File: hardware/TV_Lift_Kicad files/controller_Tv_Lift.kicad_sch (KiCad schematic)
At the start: 97 parts, among them J1 socket LAN8720a, J10 CONN_IR_OUT, J11 DRY CONTACT UP DOWN, J12 DRY CONTACT, J2 POWER 24V, J3 CAN_bus, J4 ENCODER, J5 ENCODER_POWER, J6 CONN_RS232, J7 M1 LIMIT UP DOWN, J8 Signal PWR, J9 MOTOR_OUT, Q1 2N3904, SW1 UP, SW2 DOWN, SW3 STOP, SW4 Reset, U1 MAX3232, U10 VNH5019A-E, U2 TSOP32S40F, U3 SN65HVD230, U4 ESP32-WROOM-32, U5 LM2596S-5, U6 AMS1117-3.3, U7 PC817, U8 PC817, U9 NCS1S1205SC

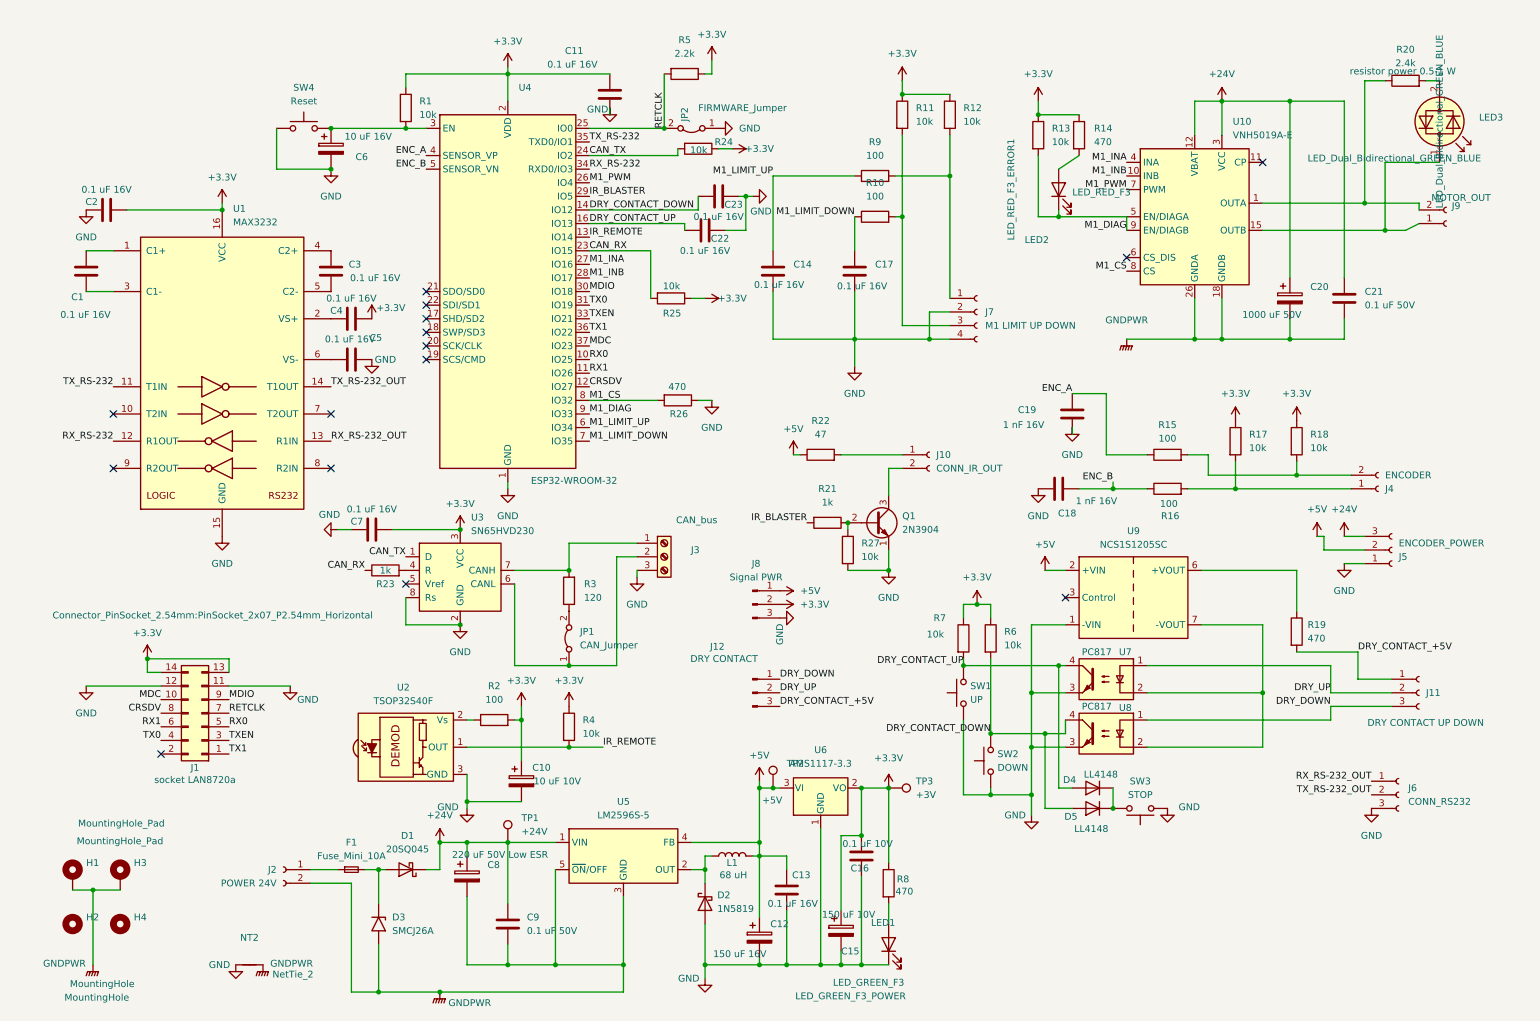
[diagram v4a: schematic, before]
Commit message: fix bom list of connectors
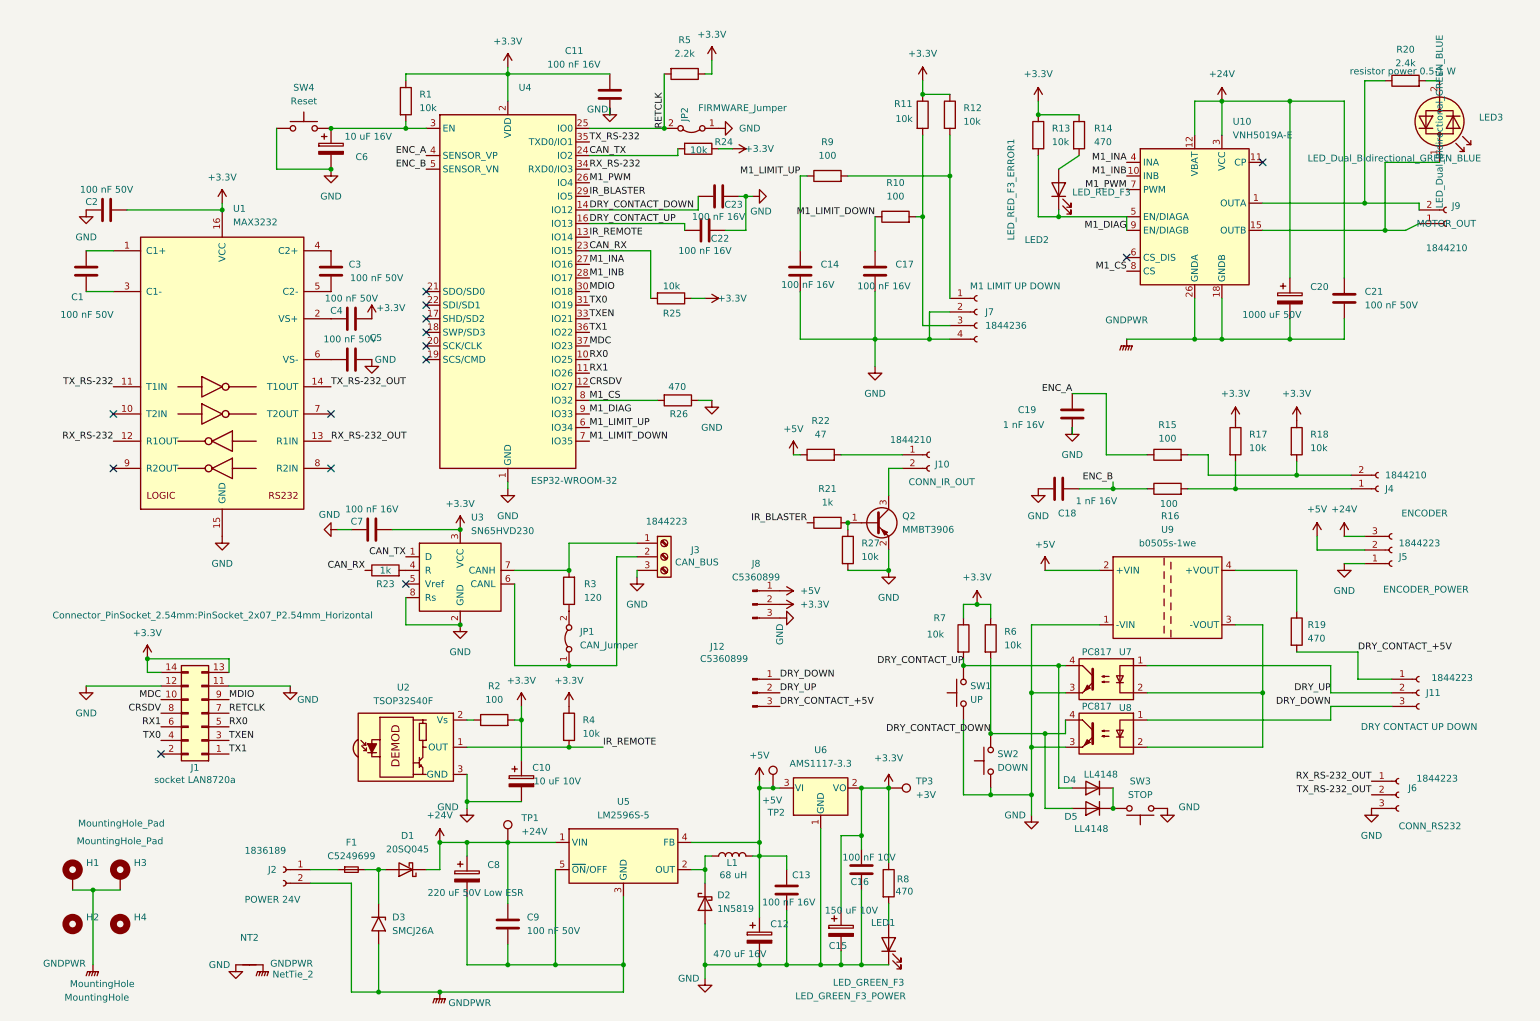
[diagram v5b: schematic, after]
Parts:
- removed Q1: 2N3904, Package_TO_SOT_THT:TO-92_Inline, symbol Transistor_BJT:2N3904
- added Q2: MMBT3906, Package_TO_SOT_SMD:SOT-23, symbol Transistor_BJT:MMBT3906
- C1, C2, C3, C4, C5: value 0.1 uF 16V -> 100 nF 50V
- C11, C13, C14, C17, C22, C23, C7: value 0.1 uF 16V -> 100 nF 16V
- C12: value 150 uF 16V -> 470 uF 16V
- C16: value 0.1 uF 10V -> 100 nF 10V
- C21, C9: value 0.1 uF 50V -> 100 nF 50V
- C6: footprint Capacitor_THT:CP_Radial_D5.0mm_P2.00mm -> Capacitor_SMD:C_0805_2012Metric
- F1: value Fuse_Mini_10A -> C5249699
- J10: value CONN_IR_OUT -> 1844210
- J11: value DRY CONTACT UP DOWN -> 1844223
- J12: value DRY CONTACT -> C5360899
- J2: value POWER 24V -> 1836189
- J3: value CAN_bus -> 1844223
- J4: value ENCODER -> 1844210
- J5: value ENCODER_POWER -> 1844223
- J6: value CONN_RS232 -> 1844223
- J7: value M1 LIMIT UP DOWN -> 1844236
- J8: value Signal PWR -> C5360899
- J9: value MOTOR_OUT -> 1844210
- U9: value NCS1S1205SC -> b0505s-1we; footprint Converter_DCDC:Converter_DCDC_Murata_NCS1SxxxxSC_THT -> Converter_DCDC:Converter_DCDC_RECOM_R-78S-0.1_THT; symbol Converter_DCDC:NCS1S1205SC -> Regulator_Switching:CRE1S0505SC
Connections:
- net GND: now also Q2.2 (E)
- net at R21.1, R27.1: now also Q2.1 (B)
- net at J10.2 (Pin_2): now also Q2.3 (C)
- net at U7.2, U8.2: now also U9.3 (-VOUT); no longer U9.7 (-VOUT)
- net at R19.1: now also U9.4 (+VOUT); no longer U9.6 (+VOUT)
- no-connect marks 15 -> 14
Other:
- moved on the sheet: C14, C16, C17, R1, R10, R11, R9

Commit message: done boardConfig.h
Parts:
- C14, C17: value 100 nF 16V -> 100 nF 50V
- C18, C19: value 1 nF 16V -> 1 nF 50V
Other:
- moved on the sheet: C14, R9
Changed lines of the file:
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@@
 	)
 	(junction
+		(at 182.88 40.64)
+		(diameter 0)
+		(color 0 0 0 0)
+	)
+	(junction
 		(at 91.44 106.68)
 		(diameter 0)
@@
 	)
 	(junction
-		(at 182.88 40.64)
-		(diameter 0)
-		(color 0 0 0 0)
-	)
-	(junction
 		(at 179.07 71.12)
 		(diameter 0)
@@
 	(wire
 		(pts
-			(xy 154.94 71.12) (xy 168.91 71.12)
+			(xy 158.75 71.12) (xy 168.91 71.12)
 		)
 		(stroke
@@
 	(wire
 		(pts
-			(xy 163.83 40.64) (xy 182.88 40.64)
+			(xy 167.64 40.64) (xy 182.88 40.64)
 		)
 		(stroke
@@
 	(wire
 		(pts
-			(xy 154.94 62.23) (xy 154.94 71.12)
+			(xy 158.75 62.23) (xy 158.75 71.12)
 		)
 		(stroke
@@
 	(wire
 		(pts
-			(xy 154.94 40.64) (xy 156.21 40.64)
+			(xy 158.75 40.64) (xy 160.02 40.64)
 		)
 		(stroke
@@
 	(wire
 		(pts
-			(xy 154.94 40.64) (xy 154.94 54.61)
+			(xy 158.75 40.64) (xy 158.75 54.61)
 		)
 		(stroke
@@
 	)
 	(label "M1_LIMIT_UP"
-		(at 154.94 40.64 180)
+		(at 158.75 40.64 180)
 		(effects
 			(font
@@
 			)
 		)
-		(property "Value" "1 nF 16V"
+		(property "Value" "1 nF 50V"
 			(at 214.122 101.346 90)
 			(show_name no)
@@
 		)
 		(property "Description" "ENCODER"
-			(at 271.526 103.632 0)
+			(at 265.938 92.202 0)
 			(show_name no)
 			(do_not_autoplace no)
@@
 			)
 		)
-		(property "Value" "1 nF 16V"
+		(property "Value" "1 nF 50V"
 			(at 192.786 87.122 0)
 			(show_name no)
@@
 	(symbol
 		(lib_id "Device:R")
-		(at 160.02 40.64 90)
+		(at 163.83 40.64 90)
 		(unit 1)
 		(body_style 1)
@@
 		(fields_autoplaced yes)
 		(property "Reference" "R9"
-			(at 160.02 34.29 90)
+			(at 163.83 34.29 90)
 			(show_name no)
 			(do_not_autoplace no)
@@
 		)
 		(property "Value" "100"
-			(at 160.02 36.83 90)
+			(at 163.83 36.83 90)
 			(show_name no)
 			(do_not_autoplace no)
@@
 		)
 		(property "Footprint" "Resistor_SMD:R_0805_2012Metric"
-			(at 160.02 42.418 90)
+			(at 163.83 42.418 90)
 			(hide yes)
 			(show_name no)
@@
 		)
 		(property "Datasheet" ""
-			(at 160.02 40.64 0)
+			(at 163.83 40.64 0)
 			(hide yes)
 			(show_name no)
@@
 		)
 		(property "Description" ""
-			(at 160.02 40.64 0)
+			(at 163.83 40.64 0)
 			(show_name no)
 			(do_not_autoplace no)
@@
 	(symbol
 		(lib_id "Device:C")
-		(at 154.94 58.42 0)
+		(at 158.75 58.42 0)
 		(unit 1)
 		(body_style 1)
@@
 		(dnp no)
 		(property "Reference" "C14"
-			(at 158.75 57.1499 0)
+			(at 166.37 57.1499 0)
 			(show_name no)
 			(do_not_autoplace no)
@@
 			)
 		)
-		(property "Value" "100 nF 16V"
-			(at 151.384 60.96 0)
+		(property "Value" "100 nF 50V"
+			(at 155.194 60.96 0)
 			(show_name no)
 			(do_not_autoplace no)
@@
 		)
 		(property "Footprint" "Capacitor_SMD:C_0805_2012Metric"
-			(at 155.9052 62.23 0)
+			(at 159.7152 62.23 0)
 			(hide yes)
 			(show_name no)
@@
 		)
 		(property "Datasheet" ""
-			(at 154.94 58.42 0)
+			(at 158.75 58.42 0)
 			(hide yes)
 			(show_name no)
@@
 		)
 		(property "Description" ""
-			(at 154.94 58.42 0)
+			(at 158.75 58.42 0)
 			(show_name no)
 			(do_not_autoplace no)
@@
 			)
 		)
-		(property "Value" "100 nF 16V"
+		(property "Value" "100 nF 50V"
 			(at 165.608 61.214 0)
 			(show_name no)

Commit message: fix input manager: correct limit switch logic and remove unnecessary comments
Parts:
- added TP4: Signal GND, TestPoint:TestPoint_Pad_D2.0mm, symbol Connector:TestPoint
- added TP5: GNDPWR, TestPoint:TestPoint_Pad_D2.0mm, symbol Connector:TestPoint
- SW1: value UP -> TS-1187A-BAB; footprint Button_Switch_THT:SW_PUSH_6mm -> Button_Switch_SMD:SW_Push_1P1T_XKB_TS-1187A
- SW2: value DOWN -> TS-1187A-BAB; footprint Button_Switch_THT:SW_PUSH_6mm -> Button_Switch_SMD:SW_Push_1P1T_XKB_TS-1187A
- SW3: value STOP -> TS-1187A-BAB; footprint Button_Switch_THT:SW_PUSH_6mm -> Button_Switch_SMD:SW_Push_1P1T_XKB_TS-1187A
- SW4: value Reset -> TS-1187A-BAB; footprint Button_Switch_THT:SW_PUSH_6mm -> Button_Switch_SMD:SW_Push_1P1T_XKB_TS-1187A
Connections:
- net GND: now also TP4.1
- net GNDPWR: now also TP5.1
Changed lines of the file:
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@@
 	)
 	(junction
-		(at 100.33 21.59)
+		(at 100.33 20.32)
 		(diameter 0)
 		(color 0 0 0 0)
@@
 	)
 	(junction
+		(at 156.21 187.96)
+		(diameter 0)
+		(color 0 0 0 0)
+	)
+	(junction
 		(at 228.6 71.12)
 		(diameter 0)
@@
 	)
 	(junction
+		(at 81.28 193.04)
+		(diameter 0)
+		(color 0 0 0 0)
+	)
+	(junction
 		(at 200.66 144.78)
 		(diameter 0)
@@
 	(wire
 		(pts
-			(xy 100.33 20.32) (xy 100.33 21.59)
-		)
-		(stroke
-			(width 0)
-			(type default)
-		)
-	)
-	(wire
-		(pts
 			(xy 144.78 50.8) (xy 140.97 50.8)
 		)
@@
 	(wire
 		(pts
-			(xy 137.16 187.96) (xy 158.75 187.96)
+			(xy 137.16 187.96) (xy 156.21 187.96)
 		)
 		(stroke
@@
 	(wire
 		(pts
-			(xy 81.28 22.86) (xy 81.28 21.59)
+			(xy 81.28 22.86) (xy 81.28 20.32)
 		)
 		(stroke
@@
 	(wire
 		(pts
-			(xy 119.38 21.59) (xy 100.33 21.59)
+			(xy 119.38 20.32) (xy 100.33 20.32)
 		)
 		(stroke
@@
 	(wire
 		(pts
-			(xy 81.28 21.59) (xy 100.33 21.59)
+			(xy 81.28 20.32) (xy 100.33 20.32)
 		)
 		(stroke
@@
 	(wire
 		(pts
+			(xy 81.28 193.04) (xy 87.63 193.04)
+		)
+		(stroke
+			(width 0)
+			(type default)
+		)
+	)
+	(wire
+		(pts
+			(xy 119.38 20.32) (xy 119.38 21.59)
+		)
+		(stroke
+			(width 0)
+			(type default)
+		)
+	)
+	(wire
+		(pts
 			(xy 71.12 193.04) (xy 76.2 193.04)
 		)
@@
 	(wire
 		(pts
+			(xy 156.21 187.96) (xy 158.75 187.96)
+		)
+		(stroke
+			(width 0)
+			(type default)
+		)
+	)
+	(wire
+		(pts
 			(xy 101.6 114.3) (xy 111.76 114.3)
 		)
@@
 	(wire
 		(pts
-			(xy 100.33 21.59) (xy 100.33 26.67)
+			(xy 100.33 20.32) (xy 100.33 26.67)
 		)
 		(stroke
@@
 	(wire
 		(pts
-			(xy 76.2 193.04) (xy 87.63 193.04)
+			(xy 76.2 193.04) (xy 81.28 193.04)
 		)
 		(stroke
@@
 		(dnp no)
 		(property "Reference" "C11"
-			(at 110.998 17.272 0)
+			(at 118.618 20.574 0)
 			(show_name no)
 			(do_not_autoplace no)
@@
 		)
 		(property "Value" "100 nF 16V"
-			(at 107.696 19.812 0)
+			(at 115.316 23.114 0)
 			(show_name no)
 			(do_not_autoplace no)
@@
 	)
 	(symbol
+		(lib_id "Connector:TestPoint")
+		(at 81.28 193.04 0)
+		(unit 1)
+		(body_style 1)
+		(exclude_from_sim no)
+		(in_bom yes)
+		(on_board yes)
+		(in_pos_files yes)
+		(dnp no)
+		(property "Reference" "TP5"
+			(at 79.502 195.072 0)
+			(show_name no)
+			(do_not_autoplace no)
+			(effects
+				(font
+					(size 1.27 1.27)
+				)
+				(justify left)
+			)
+		)
+		(property "Value" "GNDPWR"
+			(at 77.978 187.96 0)
+			(show_name no)
+			(do_not_autoplace no)
+			(effects
+				(font
+					(size 1.27 1.27)
+				)
+				(justify left)
+			)
+		)
+		(property "Footprint" "TestPoint:TestPoint_Pad_D2.0mm"
+			(at 86.36 193.04 0)
+			(hide yes)
+			(show_name no)
+			(do_not_autoplace no)
+			(effects
+				(font
+					(size 1.27 1.27)
+				)
+			)
+		)
+		(property "Datasheet" ""
+			(at 86.36 193.04 0)
+			(hide yes)
+			(show_name no)
+			(do_not_autoplace no)
+			(effects
+				(font
+					(size 1.27 1.27)
+				)
+			)
+		)
+		(property "Description" "test point"
+			(at 81.28 193.04 0)
+			(hide yes)
+			(show_name no)
+			(do_not_autoplace no)
+			(effects
+				(font
+					(size 1.27 1.27)
+				)
+			)
+		)
+		(pin "1"
+		)
+		(instances
+			(project "controller_Tv_Lift"
+				(path "/906b0219-e8e2-4a64-a5ea-d0350d472c53"
+					(reference "TP5")
+					(unit 1)
+				)
+			)
+		)
+	)
+	(symbol
 		(lib_id "Switch:SW_Push")
 		(at 62.23 31.75 0)
@@
 			)
 		)
-		(property "Value" "Reset"
+		(property "Value" "TS-1187A-BAB"
 			(at 62.23 26.67 0)
 			(show_name no)
@@
 			)
 		)
-		(property "Footprint" "Button_Switch_THT:SW_PUSH_6mm"
+		(property "Footprint" "Button_Switch_SMD:SW_Push_1P1T_XKB_TS-1187A"
 			(at 62.23 26.67 0)
 			(hide yes)
@@
 			)
 		)
-		(property "Description" "Push button switch, generic, two pins"
+		(property "Description" "RESET"
 			(at 62.23 31.75 0)
 			(hide yes)
@@
 			)
 		)
-		(property "Value" "STOP"
+		(property "Value" "TS-1187A-BAB"
 			(at 218.44 156.21 0)
 			(show_name no)
@@
 			)
 		)
-		(property "Footprint" "Button_Switch_THT:SW_PUSH_6mm"
+		(property "Footprint" "Button_Switch_SMD:SW_Push_1P1T_XKB_TS-1187A"
 			(at 218.44 163.83 0)
 			(hide yes)
@@
 			)
 		)
-		(property "Description" "Push button switch, generic, two pins"
+		(property "Description" "STOP"
 			(at 218.44 158.75 0)
 			(hide yes)
@@
 			)
 		)
-		(property "Value" "UP"
+		(property "Value" "TS-1187A-BAB"
 			(at 186.69 138.4299 90)
 			(show_name no)
@@
 			)
 		)
-		(property "Footprint" "Button_Switch_THT:SW_PUSH_6mm"
+		(property "Footprint" "Button_Switch_SMD:SW_Push_1P1T_XKB_TS-1187A"
 			(at 180.34 137.16 0)
 			(hide yes)
@@
 			)
 		)
-		(property "Description" "Push button switch, generic, two pins"
+		(property "Description" "UP"
 			(at 185.42 137.16 0)
 			(hide yes)
@@
 	)
 	(symbol
+		(lib_id "Connector:TestPoint")
+		(at 156.21 187.96 0)
+		(unit 1)
+		(body_style 1)
+		(exclude_from_sim no)
+		(in_bom yes)
+		(on_board yes)
+		(in_pos_files yes)
+		(dnp no)
+		(property "Reference" "TP4"
+			(at 154.432 189.992 0)
+			(show_name no)
+			(do_not_autoplace no)
+			(effects
+				(font
+					(size 1.27 1.27)
+				)
+				(justify left)
+			)
+		)
+		(property "Value" "Signal GND"
+			(at 149.86 191.516 0)
+			(show_name no)
+			(do_not_autoplace no)
+			(effects
+				(font
+					(size 1.27 1.27)
+				)
+				(justify left)
+			)
+		)
+		(property "Footprint" "TestPoint:TestPoint_Pad_D2.0mm"
+			(at 161.29 187.96 0)
+			(hide yes)
+			(show_name no)
+			(do_not_autoplace no)
+			(effects
+				(font
+					(size 1.27 1.27)
+				)
+			)
+		)
+		(property "Datasheet" ""
+			(at 161.29 187.96 0)
+			(hide yes)
+			(show_name no)
+			(do_not_autoplace no)
+			(effects
+				(font
+					(size 1.27 1.27)
+				)
+			)
+		)
+		(property "Description" "test point"
+			(at 156.21 187.96 0)
+			(hide yes)
+			(show_name no)
+			(do_not_autoplace no)
+			(effects
+				(font
+					(size 1.27 1.27)
+				)
+			)
+		)
+		(pin "1"
+		)
+		(instances
+			(project "controller_Tv_Lift"
+				(path "/906b0219-e8e2-4a64-a5ea-d0350d472c53"
+					(reference "TP4")
+					(unit 1)
+				)
+			)
+		)
+	)
+	(symbol
 		(lib_name "GNDPWR_2")
 		(lib_id "power:GNDPWR")
@@
 		)
 		(property "Value" "GND"
-			(at 117.094 28.194 0)
+			(at 122.428 27.686 0)
 			(show_name no)
 			(do_not_autoplace no)
@@
 			)
 		)
-		(property "Value" "DOWN"
+		(property "Value" "TS-1187A-BAB"
 			(at 191.77 151.1299 90)
 			(show_name no)
@@
 			)
 		)
-		(property "Footprint" "Button_Switch_THT:SW_PUSH_6mm"
+		(property "Footprint" "Button_Switch_SMD:SW_Push_1P1T_XKB_TS-1187A"
 			(at 185.42 149.86 0)
 			(hide yes)
@@
 			)
 		)
-		(property "Description" "Push button switch, generic, two pins"
+		(property "Description" "DOWN"
 			(at 190.5 149.86 0)
 			(hide yes)
